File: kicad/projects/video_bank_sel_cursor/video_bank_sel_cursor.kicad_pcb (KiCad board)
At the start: 2 copper layers, 203.2 x 97.8 mm, 44 parts, among them J1 peripheral_addr_bus_connector, J2 peripheral_aux_connector, J3 peripheral_membank_connector, J4 Conn_01x16_Socket, J5 Conn_01x16_Socket, J6 video_aux, J7 Conn_01x16_Socket, J8 Conn_01x06_Socket, U1 74HC245, U10 74HC10, U11 74HC377, U12 74HC377, U14 74HC245, U15 74HC245, U2 74HC245, U3 74HC245, U4 74HC245, U5 74HC245, U6 74HC245, U7 74HC245, U8 74HC245, U9 74HC10

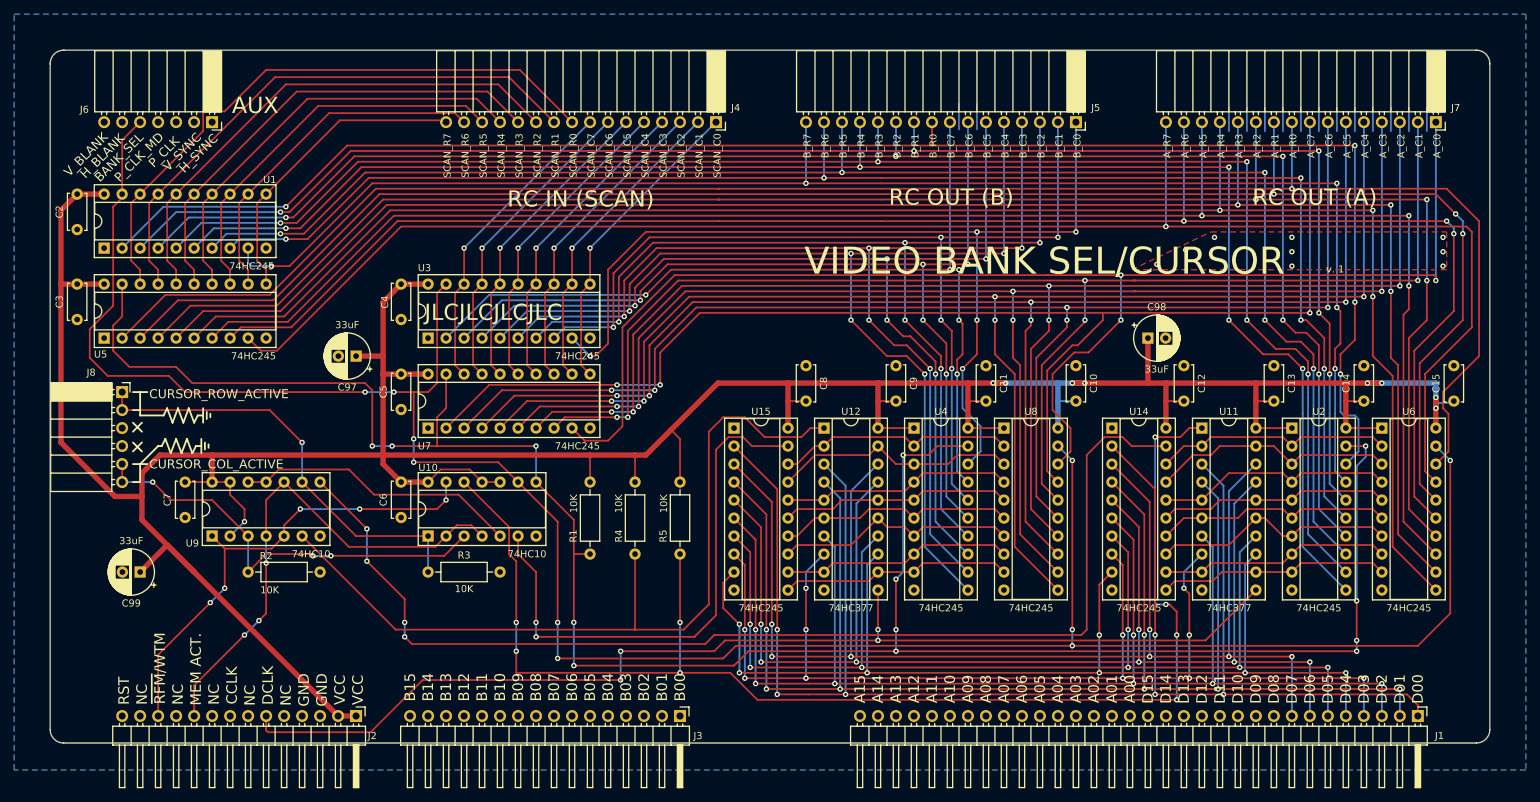
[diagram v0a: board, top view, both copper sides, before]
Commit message: Switch bank A and B positions on output and bank sel. Video output PCB mostly done.
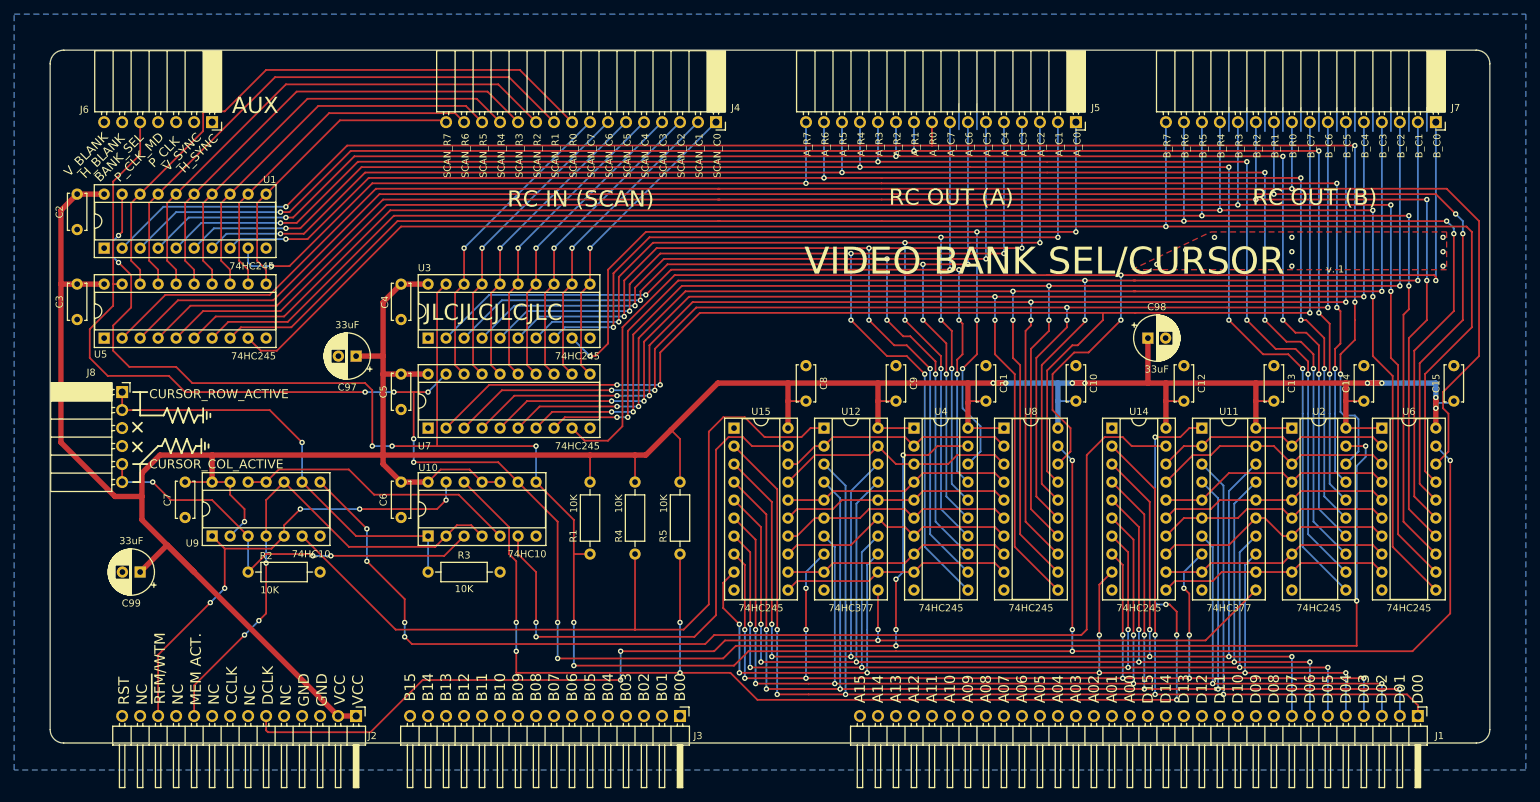
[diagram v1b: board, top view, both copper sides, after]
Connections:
- J5 pad 1: /OUT_B_COL_0 -> /OUT_A_COL_0
- J5 pad 10: /OUT_B_ROW_1 -> /OUT_A_ROW_1
- J5 pad 11: /OUT_B_ROW_2 -> /OUT_A_ROW_2
- J5 pad 12: /OUT_B_ROW_3 -> /OUT_A_ROW_3
- J5 pad 13: /OUT_B_ROW_4 -> /OUT_A_ROW_4
- J5 pad 14: /OUT_B_ROW_5 -> /OUT_A_ROW_5
- J5 pad 15: /OUT_B_ROW_6 -> /OUT_A_ROW_6
- J5 pad 16: /OUT_B_ROW_7 -> /OUT_A_ROW_7
- J5 pad 2: /OUT_B_COL_1 -> /OUT_A_COL_1
- J5 pad 3: /OUT_B_COL_2 -> /OUT_A_COL_2
- J5 pad 4: /OUT_B_COL_3 -> /OUT_A_COL_3
- J5 pad 5: /OUT_B_COL_4 -> /OUT_A_COL_4
- J5 pad 6: /OUT_B_COL_5 -> /OUT_A_COL_5
- J5 pad 7: /OUT_B_COL_6 -> /OUT_A_COL_6
- J5 pad 8: /OUT_B_COL_7 -> /OUT_A_COL_7
- J5 pad 9: /OUT_B_ROW_0 -> /OUT_A_ROW_0
- J7 pad 1: /OUT_A_COL_0 -> /OUT_B_COL_0
- J7 pad 10: /OUT_A_ROW_1 -> /OUT_B_ROW_1
- J7 pad 11: /OUT_A_ROW_2 -> /OUT_B_ROW_2
- J7 pad 12: /OUT_A_ROW_3 -> /OUT_B_ROW_3
- J7 pad 13: /OUT_A_ROW_4 -> /OUT_B_ROW_4
- J7 pad 14: /OUT_A_ROW_5 -> /OUT_B_ROW_5
- J7 pad 15: /OUT_A_ROW_6 -> /OUT_B_ROW_6
- J7 pad 16: /OUT_A_ROW_7 -> /OUT_B_ROW_7
- J7 pad 2: /OUT_A_COL_1 -> /OUT_B_COL_1
- J7 pad 3: /OUT_A_COL_2 -> /OUT_B_COL_2
- J7 pad 4: /OUT_A_COL_3 -> /OUT_B_COL_3
- J7 pad 5: /OUT_A_COL_4 -> /OUT_B_COL_4
- J7 pad 6: /OUT_A_COL_5 -> /OUT_B_COL_5
- J7 pad 7: /OUT_A_COL_6 -> /OUT_B_COL_6
- J7 pad 8: /OUT_A_COL_7 -> /OUT_B_COL_7
- J7 pad 9: /OUT_A_ROW_0 -> /OUT_B_ROW_0
- U1 pad 19: /BANK_SEL -> /~{BANK_SEL}
- U1 pad 2: /OUT_B_ROW_0 -> /OUT_A_ROW_0
- U1 pad 3: /OUT_B_ROW_1 -> /OUT_A_ROW_1
- U1 pad 4: /OUT_B_ROW_2 -> /OUT_A_ROW_2
- U1 pad 5: /OUT_B_ROW_3 -> /OUT_A_ROW_3
- U1 pad 6: /OUT_B_ROW_4 -> /OUT_A_ROW_4
- U1 pad 7: /OUT_B_ROW_5 -> /OUT_A_ROW_5
- U1 pad 8: /OUT_B_ROW_6 -> /OUT_A_ROW_6
- U1 pad 9: /OUT_B_ROW_7 -> /OUT_A_ROW_7
- U2 pad 11: /OUT_B_ROW_4 -> /OUT_A_ROW_4
- U2 pad 12: /OUT_B_ROW_3 -> /OUT_A_ROW_3
- U2 pad 13: /OUT_B_ROW_5 -> /OUT_A_ROW_5
- U2 pad 14: /OUT_B_ROW_2 -> /OUT_A_ROW_2
- U2 pad 15: /OUT_B_ROW_6 -> /OUT_A_ROW_6
- U2 pad 16: /OUT_B_ROW_1 -> /OUT_A_ROW_1
- U2 pad 17: /OUT_B_ROW_7 -> /OUT_A_ROW_7
- U2 pad 18: /OUT_B_ROW_0 -> /OUT_A_ROW_0
- U2 pad 19: /~{BANK_SEL} -> /BANK_SEL
- U3 pad 19: /BANK_SEL -> /~{BANK_SEL}
- U3 pad 2: /OUT_B_COL_7 -> /OUT_A_COL_7
- U3 pad 3: /OUT_B_COL_6 -> /OUT_A_COL_6
- U3 pad 4: /OUT_B_COL_5 -> /OUT_A_COL_5
- U3 pad 5: /OUT_B_COL_4 -> /OUT_A_COL_4
- U3 pad 6: /OUT_B_COL_3 -> /OUT_A_COL_3
- U3 pad 7: /OUT_B_COL_2 -> /OUT_A_COL_2
- U3 pad 8: /OUT_B_COL_1 -> /OUT_A_COL_1
- U3 pad 9: /OUT_B_COL_0 -> /OUT_A_COL_0
- U4 pad 11: /OUT_B_COL_4 -> /OUT_A_COL_4
- U4 pad 12: /OUT_B_COL_3 -> /OUT_A_COL_3
- U4 pad 13: /OUT_B_COL_5 -> /OUT_A_COL_5
- U4 pad 14: /OUT_B_COL_2 -> /OUT_A_COL_2
- U4 pad 15: /OUT_B_COL_6 -> /OUT_A_COL_6
- U4 pad 16: /OUT_B_COL_1 -> /OUT_A_COL_1
- U4 pad 17: /OUT_B_COL_7 -> /OUT_A_COL_7
- U4 pad 18: /OUT_B_COL_0 -> /OUT_A_COL_0
- U4 pad 19: /~{BANK_SEL} -> /BANK_SEL
- U5 pad 19: /~{BANK_SEL} -> /BANK_SEL
- U5 pad 2: /OUT_A_ROW_0 -> /OUT_B_ROW_0
- U5 pad 3: /OUT_A_ROW_1 -> /OUT_B_ROW_1
- U5 pad 4: /OUT_A_ROW_2 -> /OUT_B_ROW_2
- U5 pad 5: /OUT_A_ROW_3 -> /OUT_B_ROW_3
- U5 pad 6: /OUT_A_ROW_4 -> /OUT_B_ROW_4
- U5 pad 7: /OUT_A_ROW_5 -> /OUT_B_ROW_5
- U5 pad 8: /OUT_A_ROW_6 -> /OUT_B_ROW_6
- U5 pad 9: /OUT_A_ROW_7 -> /OUT_B_ROW_7
- U6 pad 11: /OUT_A_ROW_4 -> /OUT_B_ROW_4
- U6 pad 12: /OUT_A_ROW_3 -> /OUT_B_ROW_3
- U6 pad 13: /OUT_A_ROW_5 -> /OUT_B_ROW_5
- U6 pad 14: /OUT_A_ROW_2 -> /OUT_B_ROW_2
- U6 pad 15: /OUT_A_ROW_6 -> /OUT_B_ROW_6
- U6 pad 16: /OUT_A_ROW_1 -> /OUT_B_ROW_1
- U6 pad 17: /OUT_A_ROW_7 -> /OUT_B_ROW_7
- U6 pad 18: /OUT_A_ROW_0 -> /OUT_B_ROW_0
- U6 pad 19: /BANK_SEL -> /~{BANK_SEL}
- U7 pad 19: /~{BANK_SEL} -> /BANK_SEL
- U7 pad 2: /OUT_A_COL_7 -> /OUT_B_COL_7
- U7 pad 3: /OUT_A_COL_6 -> /OUT_B_COL_6
- U7 pad 4: /OUT_A_COL_5 -> /OUT_B_COL_5
- U7 pad 5: /OUT_A_COL_4 -> /OUT_B_COL_4
- U7 pad 6: /OUT_A_COL_3 -> /OUT_B_COL_3
- U7 pad 7: /OUT_A_COL_2 -> /OUT_B_COL_2
- U7 pad 8: /OUT_A_COL_1 -> /OUT_B_COL_1
- U7 pad 9: /OUT_A_COL_0 -> /OUT_B_COL_0
- U8 pad 11: /OUT_A_COL_4 -> /OUT_B_COL_4
- U8 pad 12: /OUT_A_COL_3 -> /OUT_B_COL_3
- U8 pad 13: /OUT_A_COL_5 -> /OUT_B_COL_5
- U8 pad 14: /OUT_A_COL_2 -> /OUT_B_COL_2
- U8 pad 15: /OUT_A_COL_6 -> /OUT_B_COL_6
- U8 pad 16: /OUT_A_COL_1 -> /OUT_B_COL_1
- U8 pad 17: /OUT_A_COL_7 -> /OUT_B_COL_7
- U8 pad 18: /OUT_A_COL_0 -> /OUT_B_COL_0
- U8 pad 19: /BANK_SEL -> /~{BANK_SEL}
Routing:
- net /OUT_B_COL_0: track 136.4 -> 197.6 mm, vias 5 -> 3
- net /OUT_A_COL_0: track 197.6 -> 136.4 mm, vias 3 -> 5
- net /OUT_B_COL_1: track 136.4 -> 194.8 mm
- net /OUT_A_COL_1: track 194.8 -> 136.4 mm
- net /OUT_B_COL_7: track 128.3 -> 186.5 mm, vias 5 -> 3
- net /OUT_A_COL_7: track 186.5 -> 128.3 mm, vias 3 -> 5
- net /OUT_B_COL_6: track 134.7 -> 191.3 mm
- net /OUT_A_COL_6: track 191.3 -> 134.7 mm
- net /OUT_B_COL_2: track 142.5 -> 197.7 mm
- net /OUT_A_COL_2: track 197.7 -> 142.5 mm
- net /OUT_B_COL_5: track 143.5 -> 196.6 mm
- net /OUT_A_COL_5: track 196.6 -> 143.5 mm
- net /OUT_B_COL_3: track 149.7 -> 202.0 mm
- net /OUT_A_COL_3: track 202.0 -> 149.7 mm
- net /OUT_B_COL_4: track 152.8 -> 204.2 mm
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
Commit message: Last few tech checks - gnd test points and video cursor/scan input switch order for vid output left to check.
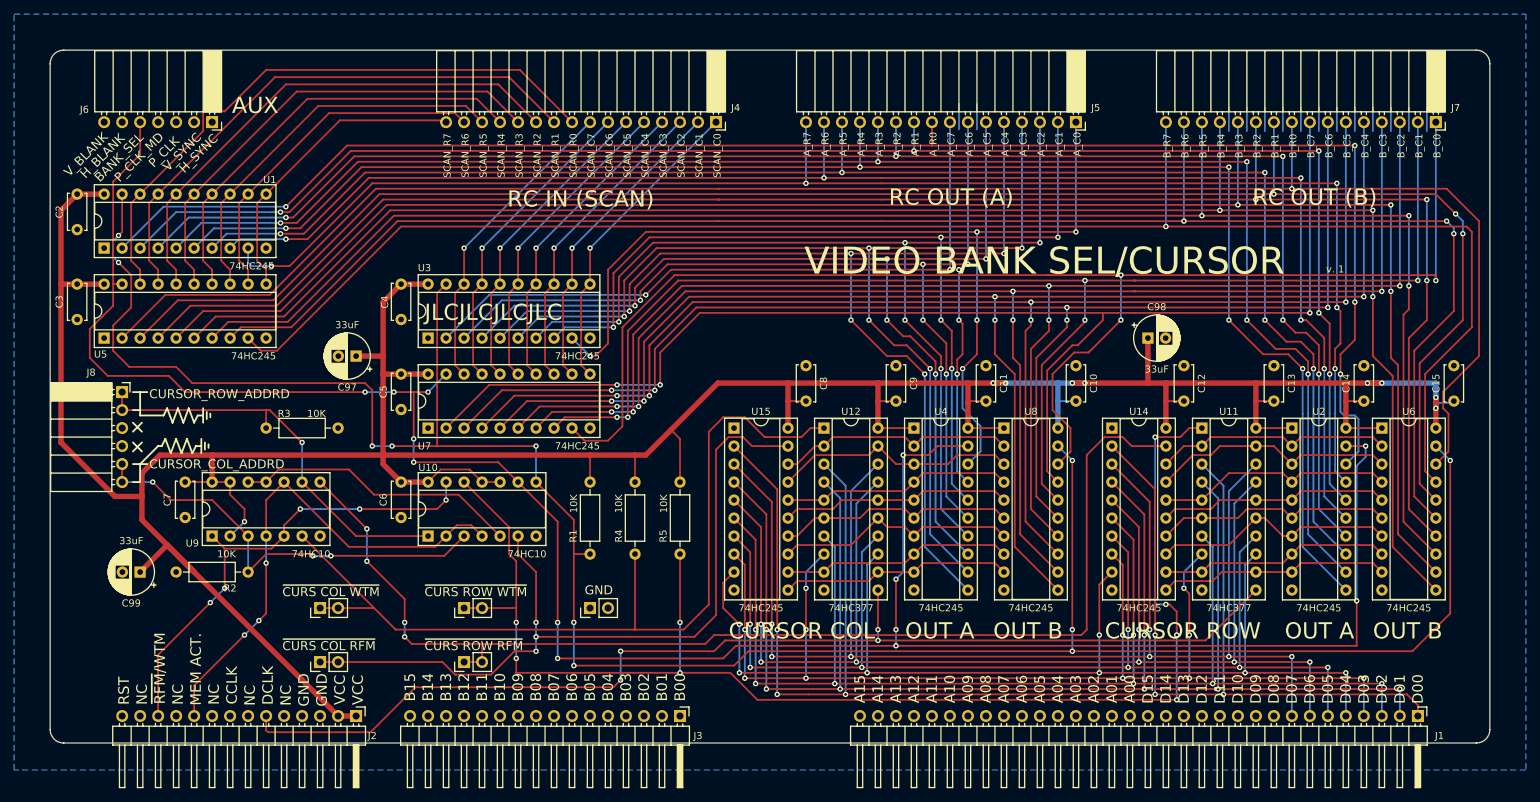
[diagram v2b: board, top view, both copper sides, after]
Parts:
- added J10: Conn_01x02_Pin, Connector_PinHeader_2.54mm:PinHeader_1x02_P2.54mm_Vertical, F.Cu at (88.9, 137.2)
- added J11: Conn_01x02_Pin, Connector_PinHeader_2.54mm:PinHeader_1x02_P2.54mm_Vertical, F.Cu at (109.2, 137.2)
- added J12: Conn_01x02_Pin, Connector_PinHeader_2.54mm:PinHeader_1x02_P2.54mm_Vertical, F.Cu at (109.2, 129.5)
- added J13: Conn_01x02_Pin, Connector_PinHeader_2.54mm:PinHeader_1x02_P2.54mm_Vertical, F.Cu at (127.0, 129.5)
- added J9: Conn_01x02_Pin, Connector_PinHeader_2.54mm:PinHeader_1x02_P2.54mm_Vertical, F.Cu at (88.9, 129.5)
- C10, C11, C12, C13, C14, C15, C2, C3, C4, C5, C6, C7, C8, C9: value C -> 0.1uF
- moved R3 30.6 mm to (81.3, 104.1)
- moved R2 20.3 mm to (68.6, 124.5), turned to 0 degrees
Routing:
- net /~{CURSOR_COL_RFM}: track 76.7 -> 111.3 mm, vias 2 -> 3
- net /~{CURSOR_COL_WTM}: track 118.2 -> 125.8 mm
- net /~{CURSOR_ROW_WTM}: track 188.1 -> 195.4 mm
- net /~{CURSOR_ROW_RFM}: track 161.7 -> 166.8 mm
- net /CURSOR_ROW_ADDRESSED: track 61.4 -> 58.9 mm
- net GND: vias 9 -> 0
- removed copper zone on F.Cu, net GND
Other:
- board text added: "CURSOR COL"
- board text added: "CURSOR ROW"
- board text added: "CURSOR_COL_ADDRD"
- board text added: "CURSOR_ROW_ADDRD"
- board text added: "GND"
- board text added: "OUT A"
- board text added: "OUT B"
- board text added: "~{CURS COL RFM}"
- board text added: "~{CURS COL WTM}"
- board text added: "~{CURS ROW RFM}"
- board text added: "~{CURS ROW WTM}"
- board text removed: "CURSOR_COL_ACTIVE"
- board text removed: "CURSOR_ROW_ACTIVE"
